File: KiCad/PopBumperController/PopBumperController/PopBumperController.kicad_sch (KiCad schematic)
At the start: 59 parts, among them J1 Conn_01x02, J10 Conn_01x03, J11 Conn_01x03, J12 Conn_01x02, J13 Conn_01x03, J14 Conn_01x02, J15 Conn_01x03, J16 Conn_01x03, J2 Conn_01x03, J3 Conn_01x02, J4 Conn_01x02, J6 Conn_01x02, J7 Conn_01x02, J8 Conn_01x02, J9 Conn_01x03, Q1 TIP102, Q10 2N3904, Q11 TIP102, Q12 TIP102, Q13 2N3904, Q14 2N3904, Q16 TIP102, Q17 TIP102, Q2 TIP102, Q3 TIP102, Q4 2N3904, Q5 2N3904, Q6 2N3904, Q7 TIP102, Q8 TIP102, Q9 2N3904, U1 Pico

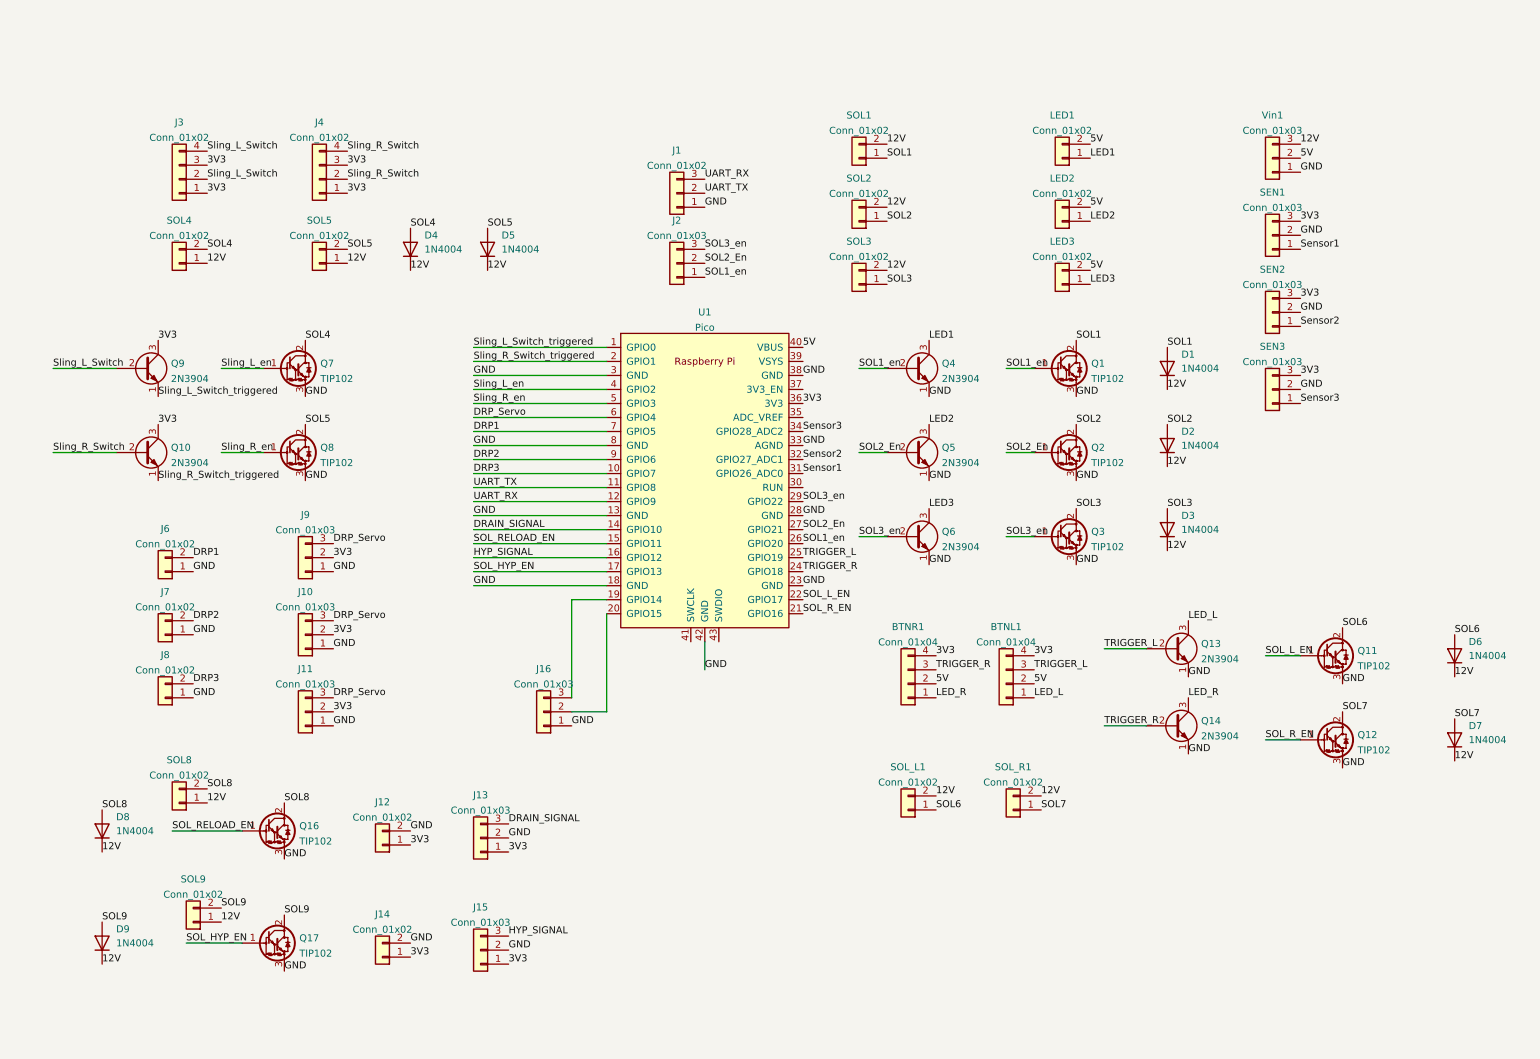
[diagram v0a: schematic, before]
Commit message: Update some CAD files, redesign solenoid controller circuit
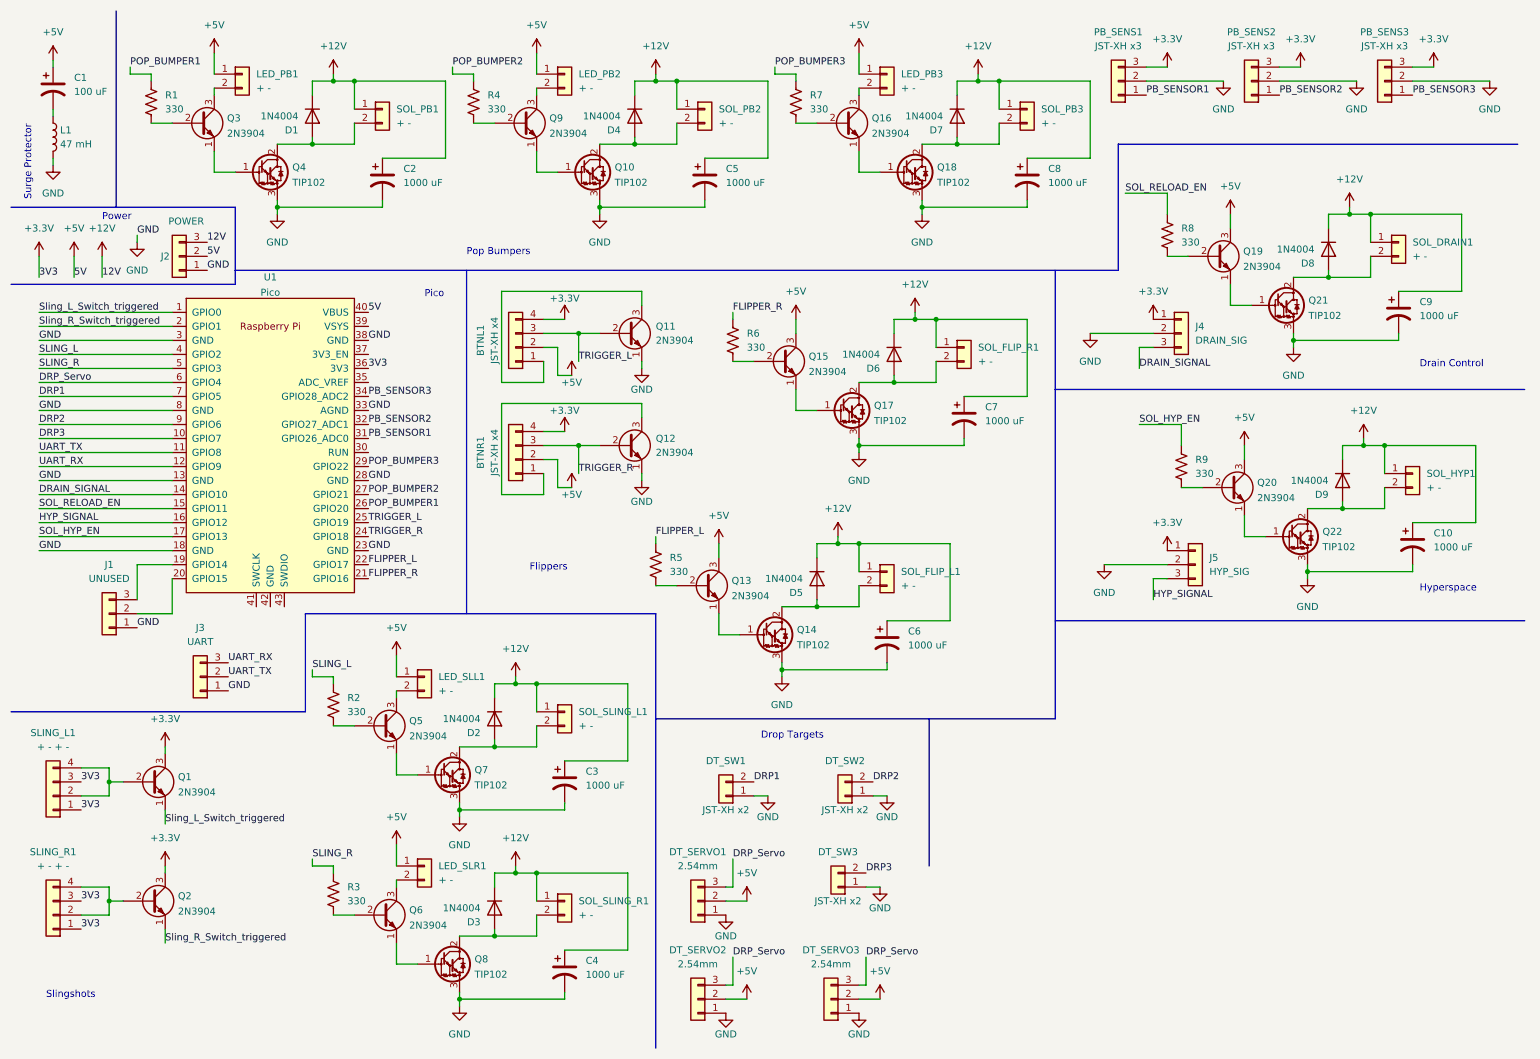
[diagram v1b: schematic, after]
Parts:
- removed J1: Conn_01x02, Connector_JST:JST_XH_B3B-XH-A_1x03_P2.50mm_Vertical, symbol Connector_Generic:Conn_01x03
- removed J10, J11, J9: Conn_01x03, Connector_PinHeader_2.54mm:PinHeader_1x03_P2.54mm_Vertical, symbol Connector_Generic:Conn_01x03
- removed J12, J14, J6, J7, J8, LED1, LED2, LED3, SOL1, SOL2, SOL3, SOL4, SOL5, SOL8, SOL9, SOL_L1, SOL_R1: Conn_01x02, Connector_JST:JST_XH_B2B-XH-A_1x02_P2.50mm_Vertical, symbol Connector_Generic:Conn_01x02
- removed J13, J15, SEN1, SEN2, SEN3, Vin1: Conn_01x03, Connector_JST:JST_XH_B3B-XH-A_1x03_P2.50mm_Vertical, symbol Connector_Generic:Conn_01x03
- removed J4: Conn_01x02, Connector_JST:JST_XH_B4B-XH-A_1x04_P2.50mm_Vertical, symbol Connector_Generic:Conn_01x04
- removed Q1, Q11, Q12, Q16, Q2, Q3: TIP102, Package_TO_SOT_THT:TO-220-3_Vertical, symbol Transistor_BJT:TIP120
- removed Q10, Q14, Q4: 2N3904, Package_TO_SOT_THT:TO-92_Inline, symbol Transistor_BJT:2N3904
- added C1: 100 uF, Capacitor_THT:CP_Radial_D8.0mm_P3.50mm, symbol Device:C_Polarized_US
- added C10, C2, C3, C4, C5, C6, C7, C8, C9: 1000 uF, Capacitor_THT:CP_Radial_D10.0mm_P5.00mm, symbol Device:C_Polarized_US
- added DT_SERVO1, DT_SERVO2, DT_SERVO3: 2.54mm, Connector_PinHeader_2.54mm:PinHeader_1x03_P2.54mm_Vertical, symbol Connector_Generic:Conn_01x03
- added DT_SW1, DT_SW2, DT_SW3: JST-XH x2, Connector_JST:JST_XH_B2B-XH-A_1x02_P2.50mm_Vertical, symbol Connector_Generic:Conn_01x02
- added J3: UART, Connector_JST:JST_XH_B3B-XH-A_1x03_P2.50mm_Vertical, symbol Connector_Generic:Conn_01x03
- added J4: DRAIN_SIG, Connector_JST:JST_XH_B3B-XH-A_1x03_P2.50mm_Vertical, symbol Connector_Generic:Conn_01x03
- added J5: HYP_SIG, Connector_JST:JST_XH_B3B-XH-A_1x03_P2.50mm_Vertical, symbol Connector_Generic:Conn_01x03
- added L1: 47 mH, Inductor_THT:L_Radial_D12.0mm_P5.00mm_Fastron_11P, symbol Device:L
- added LED_PB1, LED_PB2, LED_PB3, LED_SLL1, LED_SLR1, SOL_DRAIN1, SOL_FLIP_L1, SOL_FLIP_R1, SOL_HYP1, SOL_PB1, SOL_PB2, SOL_PB3, SOL_SLING_L1, SOL_SLING_R1: + -, Connector_JST:JST_XH_B2B-XH-A_1x02_P2.50mm_Vertical, symbol Connector_Generic:Conn_01x02
- added PB_SENS1, PB_SENS2, PB_SENS3: JST-XH x3, Connector_JST:JST_XH_B3B-XH-A_1x03_P2.50mm_Vertical, symbol Connector_Generic:Conn_01x03
- added Q1, Q11, Q12, Q15, Q16, Q19, Q2, Q20, Q3: 2N3904, Package_TO_SOT_THT:TO-92_Inline, symbol Transistor_BJT:2N3904
- added Q10, Q14, Q18, Q21, Q22, Q4: TIP102, Package_TO_SOT_THT:TO-220-3_Vertical, symbol Transistor_BJT:TIP120
- added R1, R2, R3, R4, R5, R6, R7, R8, R9: 330, Resistor_THT:R_Axial_DIN0309_L9.0mm_D3.2mm_P12.70mm_Horizontal, symbol Device:R_US
- added SLING_R1: + - + -, Connector_JST:JST_XH_B4B-XH-A_1x04_P2.50mm_Vertical, symbol Connector_Generic:Conn_01x04
- BTNL1, BTNR1: value Conn_01x04 -> JST-XH x4
- J1: renamed from J16; value Conn_01x03 -> UNUSED
- J2: value Conn_01x03 -> POWER
- SLING_L1: renamed from J3; value Conn_01x02 -> + - + -
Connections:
- net DRAIN_SIGNAL: now also J4.3 (Pin_3)
- net DRP1: now also DT_SW1.2 (Pin_2)
- net DRP2: now also DT_SW2.2 (Pin_2)
- net DRP3: now also DT_SW3.2 (Pin_2)
- net DRP_Servo: now also DT_SERVO1.3 (Pin_3), DT_SERVO2.3 (Pin_3), DT_SERVO3.3 (Pin_3)
- net GND: now also J2.1 (Pin_1), C10.2, C2.2, C3.2, C4.2, C5.2, C6.2, C7.2, C8.2, C9.2, DT_SERVO1.1 (Pin_1), DT_SERVO2.1 (Pin_1), DT_SERVO3.1 (Pin_1), DT_SW1.1 (Pin_1), DT_SW2.1 (Pin_1), DT_SW3.1 (Pin_1), J3.1 (Pin_1), J4.2 (Pin_2), J5.2 (Pin_2), L1.2, PB_SENS1.2 (Pin_2), PB_SENS2.2 (Pin_2), PB_SENS3.2 (Pin_2), Q10.3 (E), Q11.1 (E), Q12.1 (E), Q14.3 (E), Q18.3 (E), Q21.3 (E), Q22.3 (E), Q4.3 (E); no longer Q13.1 (E), Q5.1 (E), Q6.1 (E), U1.42 (GND)
- net HYP_SIGNAL: now also J5.3 (Pin_3)
- net SOL_HYP_EN: now also R9.1; no longer Q17.1 (B)
- net SOL_RELOAD_EN: now also R8.1
- net Sling_L_Switch_triggered: now also Q1.1 (E); no longer Q9.1 (E)
- net Sling_R_Switch_triggered: now also Q2.1 (E)
- net TRIGGER_L: now also Q11.2 (B); no longer Q13.2 (B)
- net TRIGGER_R: now also Q12.2 (B)
- net UART_RX: now also J3.3 (Pin_3)
- net UART_TX: now also J3.2 (Pin_2)
- net 12V renamed +12V
- net +12V: now also J2.3 (Pin_3), C10.1, C2.1, C3.1, C4.1, C5.1, C6.1, C7.1, C8.1, C9.1, SOL_DRAIN1.1 (Pin_1), SOL_FLIP_L1.1 (Pin_1), SOL_FLIP_R1.1 (Pin_1), SOL_HYP1.1 (Pin_1), SOL_PB1.1 (Pin_1), SOL_PB2.1 (Pin_1), SOL_PB3.1 (Pin_1), SOL_SLING_L1.1 (Pin_1), SOL_SLING_R1.1 (Pin_1)
- net 3V3 renamed +3V3
- net +3V3: now also J4.1 (Pin_1), J5.1 (Pin_1), PB_SENS1.3 (Pin_3), PB_SENS2.3 (Pin_3), PB_SENS3.3 (Pin_3), Q1.3 (C), Q2.3 (C), SLING_R1.1 (Pin_1), SLING_R1.3 (Pin_3); no longer Q9.3 (C)
- net 5V renamed +5V
- net +5V: now also J2.2 (Pin_2), Q13.3 (C), C1.1, DT_SERVO1.2 (Pin_2), DT_SERVO2.2 (Pin_2), DT_SERVO3.2 (Pin_2), LED_PB1.1 (Pin_1), LED_PB2.1 (Pin_1), LED_PB3.1 (Pin_1), LED_SLL1.1 (Pin_1), LED_SLR1.1 (Pin_1), Q15.3 (C), Q19.3 (C), Q20.3 (C)
- net LED2: no longer names the net of Q5.3 (C)
- net LED2: now also LED_SLL1.2 (Pin_2)
- net LED3: no longer names the net of Q6.3 (C)
- net LED3: now also LED_SLR1.2 (Pin_2)
- net LED_L: no longer names the net of BTNL1.1 (Pin_1)
- net LED_L: now also Q11.3 (C); no longer Q13.3 (C)
- net LED_R: no longer names the net of BTNR1.1 (Pin_1)
- net LED_R: now also Q12.3 (C)
- net SOL1: no longer names the net of D1.2 (A)
- net SOL1: now also Q4.2 (C), SOL_PB1.2 (Pin_2)
- net SOL1_en renamed POP_BUMPER1
- net POP_BUMPER1: now also R1.1; no longer J2.1 (Pin_1)
- net SOL2: no longer names the net of D2.2 (A)
- net SOL2: now also Q7.2 (C), SOL_SLING_L1.2 (Pin_2)
- removed net SOL2_En: J2.2 (Pin_2), Q5.2 (B), U1.27 (GPIO21)
- net SOL3: no longer names the net of D3.2 (A)
- net SOL3: now also Q8.2 (C), SOL_SLING_R1.2 (Pin_2)
- removed net SOL3_en: J2.3 (Pin_3), Q6.2 (B), U1.29 (GPIO22)
- net SOL4: no longer names the net of D4.2 (A)
- net SOL4: now also Q10.2 (C), SOL_PB2.2 (Pin_2); no longer Q7.2 (C)
- net SOL5: no longer names the net of D5.2 (A)
- net SOL5: now also Q14.2 (C), SOL_FLIP_L1.2 (Pin_2); no longer Q8.2 (C)
- net SOL6: no longer names the net of D6.2 (A)
- net SOL6: now also Q17.2 (C), SOL_FLIP_R1.2 (Pin_2)
- net SOL7: no longer names the net of D7.2 (A)
- net SOL7: now also Q18.2 (C), SOL_PB3.2 (Pin_2)
- net SOL8: no longer names the net of D8.2 (A)
- net SOL8: now also Q21.2 (C), SOL_DRAIN1.2 (Pin_2)
- net SOL9: no longer names the net of D9.2 (A)
- net SOL9: now also Q22.2 (C), SOL_HYP1.2 (Pin_2); no longer Q17.2 (C)
- net SOL_L_EN renamed FLIPPER_L
- net FLIPPER_L: now also R5.1
- net SOL_R_EN renamed FLIPPER_R
- net FLIPPER_R: now also R6.1
- net Sensor1 renamed PB_SENSOR1
- net PB_SENSOR1: now also PB_SENS1.1 (Pin_1)
- net Sensor2 renamed PB_SENSOR2
- net PB_SENSOR2: now also PB_SENS2.1 (Pin_1)
- net Sensor3 renamed PB_SENSOR3
- net PB_SENSOR3: now also PB_SENS3.1 (Pin_1)
- net Sling_L_Switch: no longer names the net of SLING_L1.2 (Pin_2), SLING_L1.4 (Pin_4)
- net Sling_L_Switch: now also Q1.2 (B); no longer Q9.2 (B)
- net Sling_L_en: no longer names the net of Q7.1 (B)
- net Sling_L_en: now also Q5.1 (E); no longer U1.4 (GPIO2)
- net Sling_R_en: no longer names the net of Q8.1 (B)
- net Sling_R_en: now also Q6.1 (E); no longer U1.5 (GPIO3)
- new net: Q13.2 (B), R5.2
- new net: Q16.2 (B), R7.2
- new net: Q20.1 (E), Q22.1 (B)
- new net: Q13.1 (E), Q14.1 (B)
- new net: Q10.1 (B), Q9.1 (E)
- new net: Q20.2 (B), R9.2
- new net: Q15.1 (E), Q17.1 (B)
- new net: Q15.2 (B), R6.2
- new net: LED_PB3.2 (Pin_2), Q16.3 (C)
- new net: Q9.2 (B), R4.2
- new net: Q6.2 (B), R3.2
- new net: LED_PB2.2 (Pin_2), Q9.3 (C)
- new net: Q5.2 (B), R2.2
- new net: C1.2, L1.1
- new net: Q16.1 (E), Q18.1 (B)
- new net: Q19.1 (E), Q21.1 (B)
- new net: Q3.1 (E), Q4.1 (B)
- new net: Q2.2 (B), SLING_R1.2 (Pin_2), SLING_R1.4 (Pin_4)
- new net: Q3.2 (B), R1.2
- new net: LED_PB1.2 (Pin_2), Q3.3 (C)
- new net: Q19.2 (B), R8.2
- new net POP_BUMPER2: R4.1, U1.27 (GPIO21)
- new net POP_BUMPER3: R7.1, U1.29 (GPIO22)
- new net SLING_L: R2.1, U1.4 (GPIO2)
- new net SLING_R: R3.1, U1.5 (GPIO3)
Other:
- note added: "Drain Control"
- note added: "Drop Targets"
- note added: "Flippers"
- note added: "Hyperspace"
- note added: "Pico"
- note added: "Pop Bumpers"
- note added: "Power"
- note added: "Slingshots"
- note added: "Surge Protector"
- moved on the sheet: J1, SLING_L1, U1

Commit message: Fix schematic issues, start PCB layout
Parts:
- added C11: 100 uF, Capacitor_THT:CP_Radial_D8.0mm_P3.50mm, symbol Device:C_Polarized_US
- added C12: 15000 uF, Capacitor_THT:CP_Radial_D25.0mm_P10.00mm_SnapIn, symbol Device:C_Polarized_US
- added J6: HYP_SIG2, Connector_JST:JST_XH_B2B-XH-A_1x02_P2.50mm_Vertical, symbol Connector_Generic:Conn_01x02
- added J7: DRAIN_SIG2, Connector_JST:JST_XH_B2B-XH-A_1x02_P2.50mm_Vertical, symbol Connector_Generic:Conn_01x02
- added R10, R11: 470k, Resistor_THT:R_Axial_DIN0309_L9.0mm_D3.2mm_P12.70mm_Horizontal, symbol Device:R_US
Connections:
- net +12V: now also C12.1, R10.1
- net +3V3: now also C11.1; no longer J4.1 (Pin_1), J5.1 (Pin_1)
- net +5V: now also J4.1 (Pin_1), J5.1 (Pin_1), J6.1 (Pin_1), J7.1 (Pin_1), R11.1
- net GND: now also C11.2, C12.2, J6.2 (Pin_2), J7.2 (Pin_2), R10.2, R11.2
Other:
- moved on the sheet: C1, L1

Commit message: placement
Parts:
- J3: footprint Connector_JST:JST_XH_B3B-XH-A_1x03_P2.50mm_Vertical -> Connector_JST:JST_XH_B2B-XH-A_1x02_P2.50mm_Vertical; symbol Connector_Generic:Conn_01x03 -> Connector_Generic:Conn_01x02
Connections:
- net GND: no longer J3.1 (Pin_1)
- net UART_RX: now also J3.2 (Pin_2); no longer J3.3 (Pin_3)
- net UART_TX: now also J3.1 (Pin_1); no longer J3.2 (Pin_2)
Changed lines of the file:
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@@
     (stroke (width 0) (type default) (color 0 0 0 0))
   )
-  (polyline (pts (xy 30.48 11.43) (xy 30.48 46.99))
-    (stroke (width 0) (type default) (color 0 0 0 0))
-  )
   (wire (pts (xy 186.69 22.86) (xy 186.69 24.13))
     (stroke (width 0) (type default) (color 0 0 0 0))
@@
     (effects (font (size 1.27 1.27)) (justify left bottom))
   )
-  (label "GND" (at 50.8 134.62 0)
-    (effects (font (size 1.27 1.27)) (justify left bottom))
-  )
   (label "DRAIN_SIGNAL" (at 16.51 99.06 0)
     (effects (font (size 1.27 1.27)) (justify left bottom))
@@
     (pin "1")
   )
-  (symbol (lib_id "Connector_Generic:Conn_01x03") (at 45.72 132.08 180) (unit 1)
+  (symbol (lib_id "Connector_Generic:Conn_01x02") (at 45.72 132.08 180) (unit 1)
     (in_bom yes) (on_board yes) (fields_autoplaced)
     (property "Reference" "J3" (id 0) (at 45.72 123.19 0))
     (property "Value" "UART" (id 1) (at 45.72 125.73 0))
-    (property "Footprint" "Connector_JST:JST_XH_B3B-XH-A_1x03_P2.50mm_Vertical" (id 2) (at 45.72 132.08 0)
+    (property "Footprint" "Connector_JST:JST_XH_B2B-XH-A_1x02_P2.50mm_Vertical" (id 2) (at 45.72 132.08 0)
       (effects (font (size 1.27 1.27)) hide)
     )
@@
     (pin "1")
     (pin "2")
-    (pin "3")
   )
   (symbol (lib_id "Device:C_Polarized_US") (at 184.15 85.09 0) (unit 1)
@@
     )
     (path "/f94b6eb3-efc8-4586-ac25-4b02e582f4f8"
-      (reference "J3") (unit 1) (value "UART") (footprint "Connector_JST:JST_XH_B3B-XH-A_1x03_P2.50mm_Vertical")
+      (reference "J3") (unit 1) (value "UART") (footprint "Connector_JST:JST_XH_B2B-XH-A_1x02_P2.50mm_Vertical")
     )
     (path "/e3e401d7-838d-4ffe-b2c7-aa8fbc80107d"
